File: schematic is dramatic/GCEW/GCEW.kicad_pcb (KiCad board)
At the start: 2 copper layers, 80 x 87 mm, 37 parts, among them Q1 Q_NMOS_DGS, Q2 Q_NMOS_DGS, Q3 Q_NMOS_DGS, Q4 Q_NMOS_DGS, Q5 Q_NMOS_DGS, Q6 Q_NMOS_DGS, U1 DRV8323RHRGZ, U2 BLDCMOTOR, U3 LM26CIM5-VHA

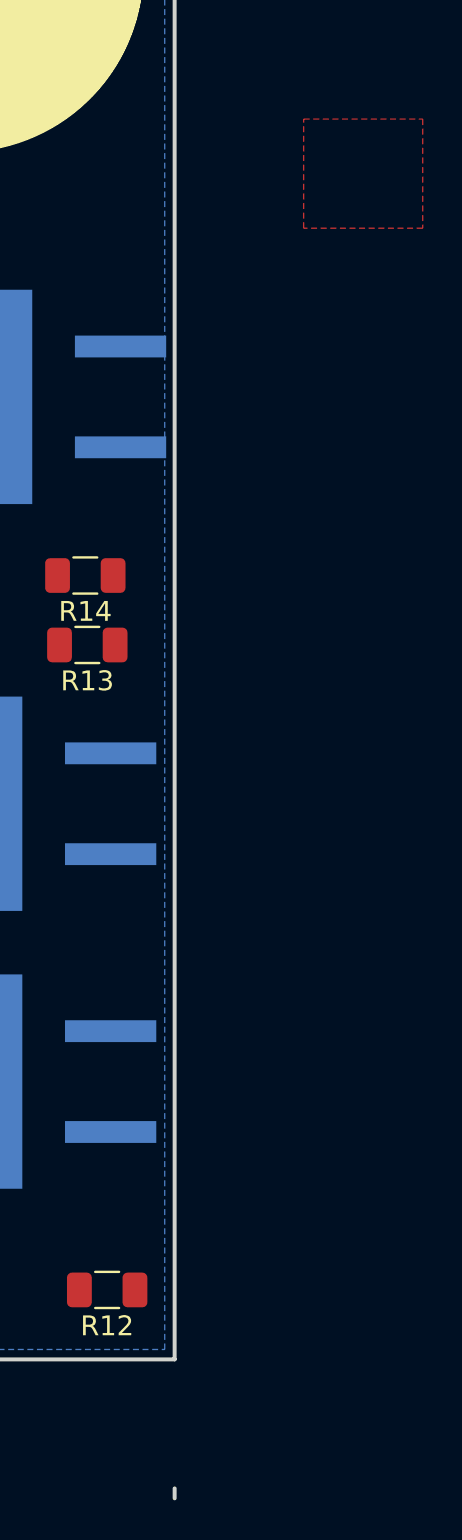
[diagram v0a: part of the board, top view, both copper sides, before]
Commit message: GCEW Motor Controller Schematic Update 1
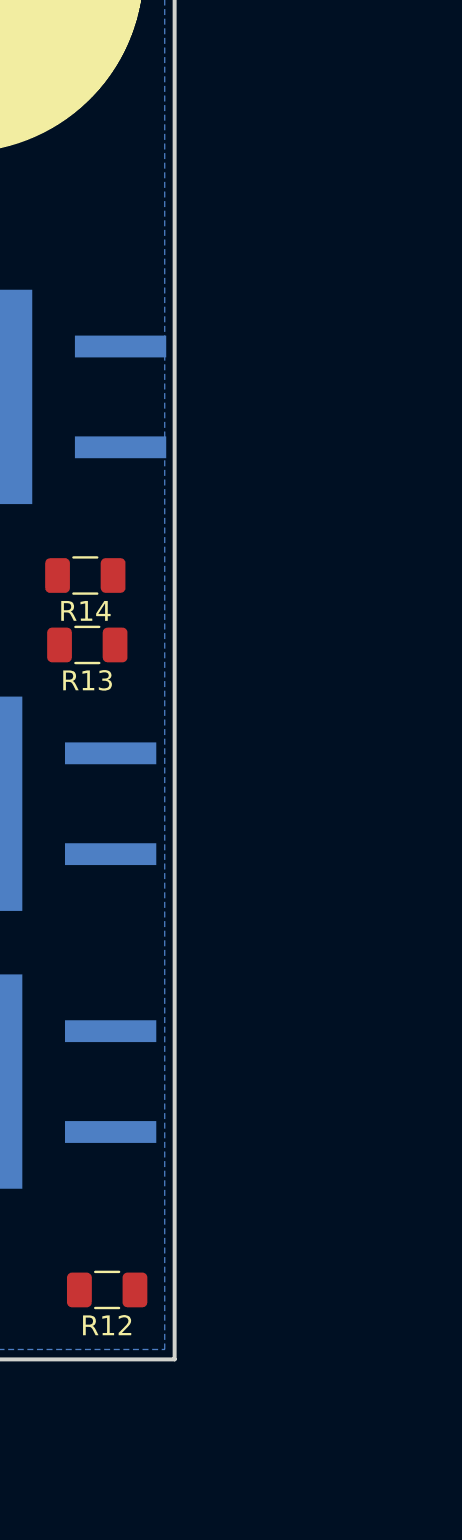
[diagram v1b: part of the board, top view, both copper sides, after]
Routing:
- removed copper zone on F.Cu, net Net-(Q5-Pad3)
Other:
- board size 80 x 87 mm -> 80 x 80 mm
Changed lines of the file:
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@@
-(kicad_pcb (version 20171130) (host pcbnew "(5.0.0)")
+(kicad_pcb (version 20171130) (host pcbnew "(5.0.1)-3")
   (general
     (thickness 1.6)
-    (drawings 5)
+    (drawings 4)
     (tracks 3)
     (zones 0)
@@
     (0 F.Cu signal)
     (31 B.Cu signal hide)
-    (32 B.Adhes user)
+    (32 B.Adhes user hide)
     (33 F.Adhes user)
     (34 B.Paste user)
     (35 F.Paste user)
-    (36 B.SilkS user)
+    (36 B.SilkS user hide)
     (37 F.SilkS user)
-    (38 B.Mask user)
-    (39 F.Mask user)
+    (38 B.Mask user hide)
+    (39 F.Mask user hide)
     (40 Dwgs.User user)
-    (41 Cmts.User user)
-    (42 Eco1.User user)
-    (43 Eco2.User user)
+    (41 Cmts.User user hide)
+    (42 Eco1.User user hide)
+    (43 Eco2.User user hide)
     (44 Edge.Cuts user)
-    (45 Margin user)
+    (45 Margin user hide)
     (46 B.CrtYd user)
     (47 F.CrtYd user)
-    (48 B.Fab user)
-    (49 F.Fab user)
+    (48 B.Fab user hide)
+    (49 F.Fab user hide)
   )
   (setup
@@
     (pad_drill 0.762)
     (pad_to_mask_clearance 0.2)
+    (solder_mask_min_width 0.25)
     (aux_axis_origin 0 0)
     (visible_elements 7FFFF7FF)
@@
   (gr_line (start 169.5 50) (end 89.5 50) (layer Edge.Cuts) (width 0.2))
   (gr_line (start 169.5 130) (end 169.5 50) (layer Edge.Cuts) (width 0.2))
-  (gr_line (start 169.5 137) (end 169.5 136.5) (layer Edge.Cuts) (width 0.2))
   (gr_line (start 89.5 130) (end 169.5 130) (layer Edge.Cuts) (width 0.2))
   (gr_line (start 89.5 50) (end 89.5 130) (layer Edge.Cuts) (width 0.2))
@@
   (segment (start 122.68 111.11) (end 122.68 112.32) (width 0.25) (layer F.Cu) (net 7))
   (segment (start 122.68 112.32) (end 122.5 112.5) (width 0.25) (layer F.Cu) (net 7))
-  (zone (net 40) (net_name "Net-(Q5-Pad3)") (layer F.Cu) (hatch edge 0.508)
-    (connect_pads (clearance 0.508))
-    (min_thickness 0.254)
-    (fill yes (arc_segments 16) (thermal_gap 0.508) (thermal_bridge_width 0.508))
-    (polygon
-      (pts
-        (xy 182 67.5) (xy 182 73) (xy 176 73) (xy 176 67.5)
-      )
-    )
-  )
   (zone (net 7) (net_name GND) (layer B.Cu) (hatch edge 0.508)
     (connect_pads (clearance 0.508))

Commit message: GCEW Motor Controller Schematic Update 5
Finalized KiCAD GCEW Motor Controller Schematic. Initial KiCAD Motor Controller PCB Design.
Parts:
- removed Q1, Q2, Q3, Q4, Q5, Q6: Q_NMOS_DGS, Package_TO_SOT_SMD:TO-263-2
- removed VDC1: 36V, TerminalBlock:TerminalBlock_Altech_AK300-3_P5.00mm
- added BT1: Battery, myLib:PhoenixContact_1935776_2-Pin-Connector_32A_P5mm, F.Cu at (174.0, 71.0)
- added C12: 4.7uF 80V, myLib:CP_Elec_6.6x6.6mm, F.Cu at (131.0, 107.0)
- added C13: 0.1uF 25V, Capacitors_SMD:C_1206, F.Cu at (145.9, 128.4)
- added C14: 0.1uF 25V, Capacitors_SMD:C_1206, F.Cu at (132.0, 142.0)
- added C15: 15uF 25V, myLib:CP_Tantalum_Case-3528, F.Cu at (127.4, 127.8)
- added J1: Conn_01x08, myLib:PhoenixContact_1985027_8-Pin-Connector_8A_P3.5mm, F.Cu at (131.0, 72.0)
- added J2: Conn_01x02, myLib:PhoenixContact_1984963_2-Pin-Connector_8A_P3.5mm, F.Cu at (122.0, 119.0)
- added J3: Conn_02x03_Odd_Even, Pin_Headers:Pin_Header_Straight_2x03_Pitch2.54mm, F.Cu at (141.0, 86.0)
- added J4: Conn_02x03_Odd_Even, Pin_Headers:Pin_Header_Straight_2x03_Pitch2.54mm, F.Cu at (150.0, 86.0)
- added J5: Conn_02x02_Odd_Even, Pin_Headers:Pin_Header_Straight_2x02_Pitch2.54mm, F.Cu at (156.0, 86.0)
- added M1: BLDC_Motor, myLib:PhoenixContact_1991309_3-Pin-Connector_32A_P5mm, F.Cu at (199.0, 111.0)
- added R15: 57.6K, Resistors_SMD:R_0805, F.Cu at (141.0, 113.0)
- added R16: 10.4K, Resistors_SMD:R_0805, F.Cu at (153.0, 131.0)
- added R17: 2milli, Resistors_SMD:R_2512, F.Cu at (255.0, 108.3)
- added R18: 2milli, Resistors_SMD:R_2512, F.Cu at (275.6, 70.9)
- added R19: 2milli, Resistors_SMD:R_2512, F.Cu at (211.8, 122.8)
- added U4: IPB029N06N, myLib:TO-263-2, F.Cu at (240.8, 108.3)
- added U5: IPB029N06N, myLib:TO-263-2, F.Cu at (236.5, 79.2)
- added U6: IPB029N06N, myLib:TO-263-2, F.Cu at (259.3, 78.7)
- added U7: IPB029N06N, myLib:TO-263-2, F.Cu at (177.5, 129.4)
- added U8: IPB029N06N, myLib:TO-263-2, F.Cu at (198.8, 129.4)
- added U9: BLDC_Hall_Sensor, myLib:PhoenixContact_1984992_5-Pin-Connector_8A_P3.5mm, F.Cu at (157.0, 72.0)
- C1: footprint Capacitor_THT:CP_Radial_D18.0mm_P7.50mm -> Capacitors_THT:CP_Radial_D18.0mm_P7.50mm
- C10: value 15uF -> 0.1uF 100V; footprint 25TQC15MYFB:CAPPM3528X200N -> Capacitors_SMD:C_1206
- C11: value 100nF -> 1uF 50V; footprint Capacitor_SMD:C_1206_3216Metric -> Capacitors_SMD:C_1206
- C2: value 1uF -> 1uF 50V; footprint Capacitor_SMD:C_1206_3216Metric -> Capacitors_SMD:C_1206
- C3: value 47nF -> 0.1uF 25V; footprint Capacitor_SMD:C_1206_3216Metric -> Capacitors_SMD:C_1206
- C4: value 100nF -> 0.1uF 25V; footprint Capacitor_SMD:C_1206_3216Metric -> Capacitors_SMD:C_1206
- C5, C6, C7: footprint Capacitor_SMD:C_1206_3216Metric -> Capacitors_SMD:C_0805
- C8: value 100nF -> 47nF 250V; footprint Capacitor_SMD:C_1206_3216Metric -> Capacitors_SMD:C_1206
- C9: value 4.7uF -> 33uF 100V; footprint CAPAE430X550N:CAPAE430X550N -> Capacitors_THT:CP_Radial_D10.0mm_P5.00mm
- D1: footprint SOT1061:SOT1061 -> Diodes_SMD:D_SOD-123F
- L1: footprint CLF10060NIT-1R0N-D:INDPM101100X630N -> myLib:CLF10060NIT-221M-D
- R1, R2: value 10k -> 10K; footprint Resistor_SMD:R_1206_3216Metric -> Resistors_SMD:R_1206
- R10: value 10.4k -> 47K; footprint Resistor_SMD:R_0805_2012Metric -> Resistors_SMD:R_1206
- R11: value 57.6k -> 10K; footprint Resistor_SMD:R_0402_1005Metric -> Resistors_SMD:R_1206
- R12: value 2m -> 10K; footprint Resistor_SMD:R_1206_3216Metric -> Resistors_SMD:R_1206
- R13: value 2m -> 1M; footprint Resistor_SMD:R_1206_3216Metric -> Resistors_SMD:R_1206
- R14: value 2m -> 100K; footprint Resistor_SMD:R_1206_3216Metric -> Resistors_SMD:R_1206
- R3: value 10k -> 18K; footprint Resistor_SMD:R_1206_3216Metric -> Resistors_SMD:R_1206
- R4: value 1M -> 75K; footprint Resistor_SMD:R_1206_3216Metric -> Resistors_SMD:R_1206
- R5: value 18k -> 1M; footprint Resistor_SMD:R_1206_3216Metric -> Resistors_SMD:R_1206
- R6: value 18k -> 75K; footprint Resistor_SMD:R_1206_3216Metric -> Resistors_SMD:R_1206
- R7: value 1M -> 18K; footprint Resistor_SMD:R_1206_3216Metric -> Resistors_SMD:R_1206
- R8: value 100k -> 10K; footprint Resistor_SMD:R_1206_3216Metric -> Resistors_SMD:R_1206
- R9: value 100k -> 1M; footprint Resistor_SMD:R_1206_3216Metric -> Resistors_SMD:R_1206
- U1: value DRV8323RHRGZ -> LM26CIM5-VHA; footprint myLib:TI-RGZ-QFN-48-1EP_7x7mm_Pitch0.5mm -> myLib:SOT-23-5
- U2: value BLDCMOTOR -> DRV8323RH; footprint TerminalBlock:TerminalBlock_Altech_AK300-3_P5.00mm -> myLib:TI-RGZ-QFN-48-1EP_7x7mm_Pitch0.5mm
- U3: value LM26CIM5-VHA -> IPB029N06N; footprint Package_TO_SOT_SMD:SOT-23-5 -> myLib:TO-263-2
- moved U1 116.9 mm to (238.8, 89.2), turned to 0 degrees
- moved U3 83.1 mm to (220.0, 108.8), turned to 180 degrees
- moved D1 82.3 mm to (142.6, 151.0)
- moved U2 77.8 mm to (155.4, 104.6), turned to 90 degrees
- moved R5 71.1 mm to (147.6, 143.3)
- moved C10 69.0 mm to (126.0, 139.0), turned to 0 degrees
- moved R9 68.8 mm to (159.0, 131.0), turned to 0 degrees
- moved R6 67.0 mm to (125.0, 143.0), turned to 0 degrees
- moved R8 62.6 mm to (139.0, 142.0), turned to 0 degrees
- moved R7 59.7 mm to (155.0, 124.0), turned to 0 degrees
- moved R2 54.7 mm to (171.0, 83.2), turned to 180 degrees
- moved C8 54.5 mm to (133.3, 134.4), turned to 0 degrees
- moved R14 50.1 mm to (157.0, 140.0), turned to 0 degrees
- moved R13 47.5 mm to (150.0, 139.0), turned to 0 degrees
- moved C6 47.3 mm to (149.0, 149.0), turned to 0 degrees
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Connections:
- C1 pad 1: +BATT -> 36V
- C1 pad 2: GND -> SNA
- C10 pad 1: GND -> 36V
- C10 pad 2: 5V -> SNA
- C11 pad 2: Net-(C11-Pad2) -> 36V
- C2 pad 1: +BATT -> DVDD
- C2 pad 2: Net-(C2-Pad2) -> SNA
- C3 pad 1: Net-(C3-Pad1) -> SNA
- C3 pad 2: Net-(C3-Pad2) -> VREF
- C4 pad 1: GND -> DVDD
- C4 pad 2: Net-(C4-Pad2) -> SNA
- C5 pad 1: GND -> Hall_A
- C5 pad 2: H_C -> SNA
- C6 pad 1: GND -> Hall_B
- C6 pad 2: H_B -> SNA
- C7 pad 1: GND -> Hall_C
- C7 pad 2: H_A -> SNA
- C8 pad 1: VCC -> Net-(C8-Pad1)
- C8 pad 2: GNDA -> Net-(C8-Pad2)
- C9 pad 1: GND -> 36V
- C9 pad 2: +BATT -> SNA
- D1 pad 1: Net-(C11-Pad2) -> Net-(C14-Pad2)
- D1 pad 2: Net-(D1-Pad2) -> SNA
- L1 pad 1: Net-(C11-Pad2) -> Net-(C14-Pad2)
- L1 pad 2: 5V -> VREF
- R1 pad 1: Net-(C4-Pad2) -> VREF
- R1 pad 2: H_C -> ENABLE
- R10 pad 1: Net-(R10-Pad1) -> Net-(J5-Pad3)
- R10 pad 2: Net-(R10-Pad2) -> GNDA
- R11 pad 1: 5V -> DVDD
- R11 pad 2: Net-(R10-Pad1) -> Net-(R11-Pad2)
- R12 pad 1: Net-(Q2-Pad3) -> DVDD
- R12 pad 2: GND -> Hall_C
- R13 pad 1: Net-(Q4-Pad3) -> Net-(R13-Pad1)
- R13 pad 2: Net-(R13-Pad2) -> GNDA
- R14 pad 1: Net-(Q6-Pad3) -> Net-(R14-Pad1)
- R14 pad 2: GND -> 36V
- R2 pad 1: Net-(C4-Pad2) -> DVDD
- R2 pad 2: H_B -> Hall_A
- R3 pad 1: Net-(C4-Pad2) -> Net-(J3-Pad1)
- R3 pad 2: H_A -> DVDD
- R4 pad 1: GNDA -> Net-(J3-Pad3)
- R4 pad 2: Net-(R4-Pad2) -> DVDD
- R5 pad 1: Net-(C4-Pad2) -> Net-(J3-Pad5)
- R5 pad 2: Net-(R5-Pad2) -> GNDA
- R6 pad 1: GNDA -> Net-(J4-Pad1)
- R6 pad 2: Net-(R6-Pad2) -> GNDA
- R7 pad 1: GNDA -> Net-(J4-Pad3)
- R7 pad 2: Net-(R7-Pad2) -> GNDA
- R8 pad 1: VCC -> DVDD
- R8 pad 2: Net-(R8-Pad2) -> Hall_B
- R9 pad 1: +BATT -> Net-(J5-Pad1)
- R9 pad 2: Net-(R9-Pad2) -> GNDA
- U1 pad 1: Net-(R10-Pad1) -> SNA
- U1 pad 2: GND -> SNA
- U1 pad 3: Net-(C3-Pad2) -> Net-(U1-Pad3)
- U1 pad 4: Net-(C3-Pad1) -> VREF
- U1 pad 5: Net-(C2-Pad2) -> ENABLE
- U2 pad 1: (no net) -> Net-(R15-Pad2)
- U2 pad 2: (no net) -> SNA
- U2 pad 3: (no net) -> Net-(C8-Pad1)
- U3 pad 1: GND -> GHA
- U3 pad 2: GND -> 36V
- U3 pad 3: Net-(U3-Pad3) -> Net-(M1-Pad1)
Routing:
- net GND: track 1.46 -> 0.00 mm, vias 1 -> 0
- removed copper zone on B.Cu, net GND
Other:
- board size 80 x 80 mm -> 90 x 90 mm
- rule pad_to_mask_clearance: 0.2 -> 0

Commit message: GCEW Motor Controller Schematic Update 5
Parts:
- R17, R18, R19, U4, U6, U8: moved to B.Cu
- moved R18 84.5 mm to (203.1, 114.2)
- moved U6 75.4 mm to (191.9, 112.5)
- moved U5 66.6 mm to (181.5, 116.8)
- moved L1 63.5 mm to (99.5, 150.2), turned to 180 degrees
- moved R5 62.9 mm to (126.2, 84.2), turned to 0 degrees
- moved R14 60.5 mm to (96.9, 132.6), turned to 180 degrees
- moved U9 58.5 mm to (122.1, 119.0), turned to 270 degrees
- moved R17 58.3 mm to (202.9, 134.6), turned to 90 degrees
- moved U4 54.8 mm to (191.8, 132.8)
- moved D1 54.5 mm to (89.6, 138.4), turned to 135 degrees
- moved R13 53.3 mm to (148.3, 85.7), turned to 135 degrees
- moved R3 53.0 mm to (126.2, 89.5)
- moved R12 52.5 mm to (132.8, 126.9), turned to 90 degrees
- moved R2 48.4 mm to (132.6, 112.6), turned to 270 degrees
- moved U3 47.9 mm to (181.4, 137.2)
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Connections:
- C13 pad 2: GNDA -> SNA
- J4 pad 5: GNDA -> SNA
- R10 pad 2: GNDA -> SNA
- R13 pad 2: GNDA -> SNA
- R5 pad 2: GNDA -> SNA
- R6 pad 2: GNDA -> SNA
- R7 pad 2: GNDA -> SNA
- R9 pad 2: GNDA -> SNA
- U1 pad 3: Net-(U1-Pad3) -> (no net)
- U2 pad 35: GNDA -> SNA
- U2 pad 46: Net-(U2-Pad46) -> (no net)
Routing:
- net SPA: track 0.00 -> 72.1 mm, vias 0 -> 3
- net Net-(M1-Pad1): track 0.00 -> 66.9 mm, vias 0 -> 32
- net SPB: track 0.00 -> 57.7 mm, vias 0 -> 1
- net GHA: track 0.00 -> 56.3 mm
- net GLA: track 0.00 -> 54.6 mm, vias 0 -> 1
- net GHB: track 0.00 -> 45.4 mm, vias 0 -> 2
- net SPC: track 0.00 -> 44.1 mm, vias 0 -> 1
- net Net-(M1-Pad2): track 0.00 -> 41.7 mm, vias 0 -> 32
- net VREF: track 0.00 -> 41.6 mm, vias 0 -> 4
- net GLB: track 0.00 -> 37.0 mm, vias 0 -> 1
- net ENABLE: track 0.00 -> 30.4 mm, vias 0 -> 4
- net GHC: track 0.00 -> 27.4 mm, vias 0 -> 2
- net Net-(M1-Pad3): track 0.00 -> 22.6 mm, vias 0 -> 31
- net SNA: track 0.00 -> 17.3 mm, vias 0 -> 16
- net Hall_C: track 0.00 -> 10.8 mm
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- added copper zone on F.Cu, net 36V
- added copper zone on F.Cu, net Net-(M1-Pad1)
- added copper zone on F.Cu, net Net-(M1-Pad2)
- added copper zone on F.Cu, net Net-(M1-Pad3)
- added copper zone on B.Cu, net SNA
- added copper zone on B.Cu, net SPA
- added copper zone on B.Cu, net SPB
- added copper zone on B.Cu, net SPC
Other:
- board size 90 x 90 mm -> 100 x 90 mm
- net class Default: clearance 0.2 -> 0.18
- rule trace_clearance: 0.2 -> 0.18

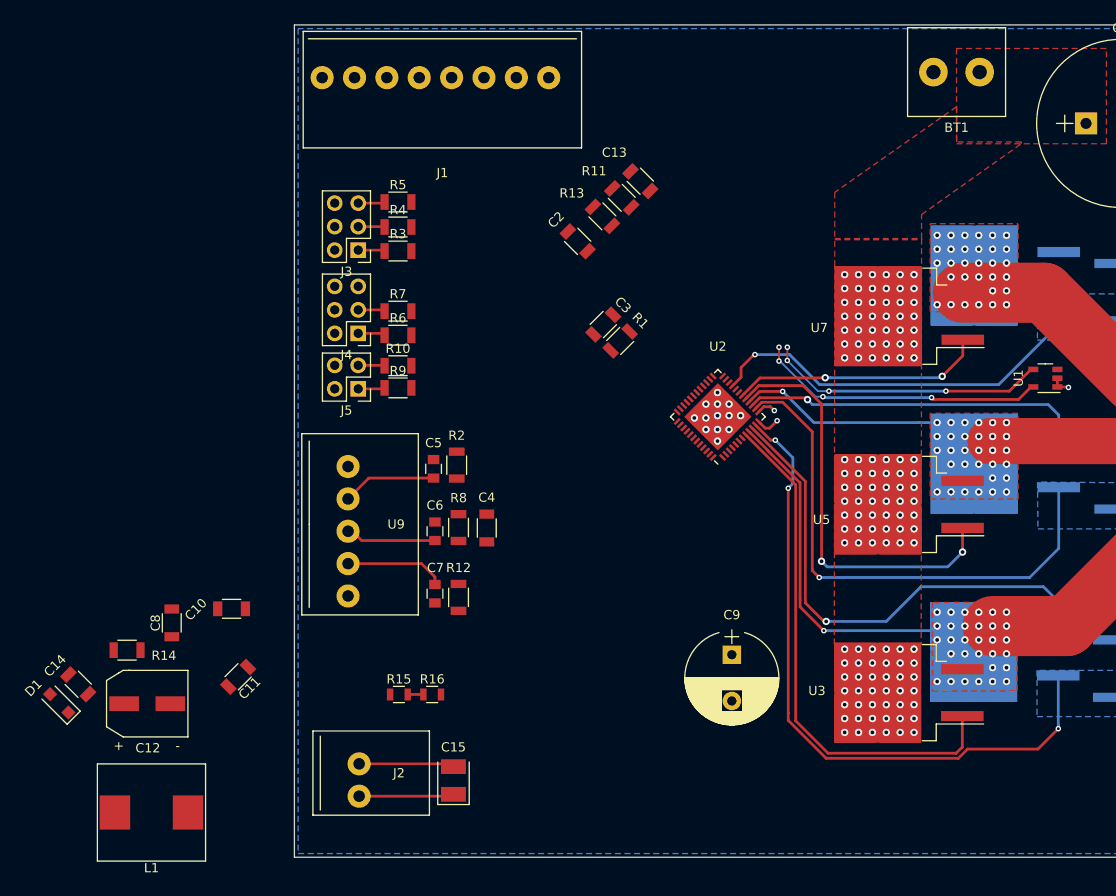
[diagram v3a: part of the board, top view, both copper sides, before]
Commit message: GCEW Motor Controller PCB Update 1
17 Connections left to complete. Still need to finalize board outline dimensions.
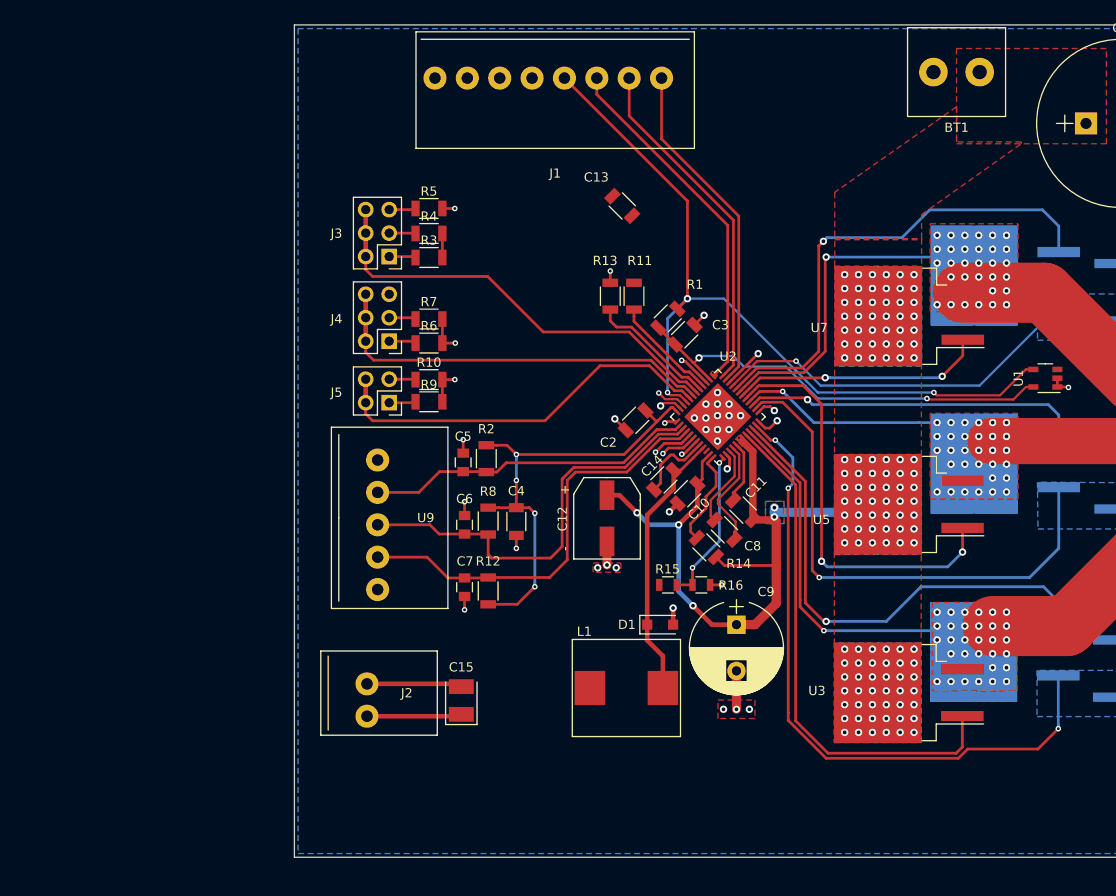
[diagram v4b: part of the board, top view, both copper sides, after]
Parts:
- moved C14 67.1 mm to (154.9, 114.2), turned to 45 degrees
- moved D1 65.5 mm to (154.6, 129.8), turned to 0 degrees
- moved R14 63.6 mm to (159.6, 121.5), turned to 315 degrees
- moved C8 60.6 mm to (161.5, 119.6), turned to 315 degrees
- moved C11 57.5 mm to (163.5, 117.5), turned to 315 degrees
- moved C12 53.6 mm to (148.8, 118.3), turned to 180 degrees
- moved L1 53.1 mm to (150.9, 136.7), turned to 0 degrees
- moved C10 50.9 mm to (157.5, 115.7), turned to 225 degrees
- moved R15 31.4 mm to (155.4, 125.5)
- moved R16 31.4 mm to (159.0, 125.5)
- moved C2 20.3 mm to (151.9, 107.8), turned to 225 degrees
- moved J1 12.2 mm to (143.2, 72.0)
- moved R11 10.7 mm to (151.7, 94.3), turned to 270 degrees
- moved C3 8.87 mm to (157.2, 98.5), turned to 225 degrees
- moved J2 8.69 mm to (124.2, 137.2)
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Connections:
- J1 pad 1: ENABLE -> SOC
- J1 pad 2: SOA -> SOB
- J1 pad 3: SOB -> SOA
- J1 pad 4: SOC -> ENABLE
- U1 pad 3: (no net) -> Net-(U1-Pad3)
- U2 pad 46: (no net) -> Net-(U2-Pad46)
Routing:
- net 36V: track 0.00 -> 74.1 mm, vias 126 -> 131
- net ENABLE: track 30.4 -> 87.6 mm, vias 4 -> 3
- net GLC: track 0.00 -> 53.2 mm, vias 0 -> 1
- net DVDD: track 0.00 -> 52.6 mm, vias 0 -> 4
- net IDRIVE: track 0.00 -> 47.8 mm
- net SNA: track 17.3 -> 62.3 mm, vias 16 -> 40
- net VDS: track 0.00 -> 43.7 mm
- net GAIN: track 0.00 -> 43.1 mm
- net SOA: track 0.00 -> 38.7 mm
- net Net-(M1-Pad3): track 22.6 -> 60.8 mm, vias 31 -> 32
- net SOB: track 0.00 -> 37.4 mm
- net SOC: track 0.00 -> 36.6 mm
- net Hall_B: track 9.81 -> 45.9 mm
- net Hall_C: track 10.8 -> 46.0 mm
- net Net-(C14-Pad2): track 0.00 -> 29.7 mm
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- added copper zone on B.Cu, net 36V
- added copper zone on F.Cu, net SNA
- added copper zone on F.Cu, net SOA
